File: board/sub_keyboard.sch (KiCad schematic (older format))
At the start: 30 parts, among them SW901 SW_SPST, SW902 SW_SPST, SW903 SW_SPST, SW904 SW_SPST, SW905 SW_SPST, SW906 SW_SPST, SW907 SW_SPST, SW908 SW_SPST, SW909 SW_SPST, SW910 SW_SPST, SW911 SW_SPST, SW912 SW_SPST, SW913 SW_SPST, SW914 SW_SPST, SW915 SW_SPST, SW916 SW_SPST, SW917 SW_SPST, SW918 SW_SPST, SW919 SW_SPST, SW920 SW_SPST, SW921 SW_SPST, SW922 SW_SPST, SW923 SW_SPST, SW924 SW_SPST, SW925 SW_SPST, SW926 SW_SPST, SW927 SW_SPST, SW928 SW_SPST, SW929 SW_SPST, SW930 SW_SPST

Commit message: Started picking footprints. Merged many components.
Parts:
- SW901, SW902, SW903, SW904, SW905, SW906, SW907, SW908, SW909, SW910, SW911, SW912, SW913, SW914, SW915, SW916, SW917, SW918, SW919, SW920, SW921, SW922, SW923, SW924, SW925, SW926, SW927, SW928, SW929, SW930: footprint (none) -> Button_Switch_Keyboard:SW_Cherry_MX1A_1.00u_PCB
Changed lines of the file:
@@
 $Descr A4 11693 8268
 encoding utf-8
-Sheet 9 14
+Sheet 9 15
 Title ""
 Date ""
@@
 F 0 "SW901" H 4500 2450 50  0000 L CNN
 F 1 "SW_SPST" H 4450 2350 50  0001 L CNN
-F 2 "" H 4600 2500 50  0001 C CNN
+F 2 "Button_Switch_Keyboard:SW_Cherry_MX1A_1.00u_PCB" H 4600 2500 50  0001 C CNN
 F 3 "" H 4600 2500 50  0001 C CNN
 	1    4600 2500
@@
 F 0 "SW902" H 5150 2450 50  0000 L CNN
 F 1 "SW_SPST" H 5100 2350 50  0001 L CNN
-F 2 "" H 5250 2500 50  0001 C CNN
+F 2 "Button_Switch_Keyboard:SW_Cherry_MX1A_1.00u_PCB" H 5250 2500 50  0001 C CNN
 F 3 "" H 5250 2500 50  0001 C CNN
 	1    5250 2500
@@
 F 0 "SW903" H 5800 2450 50  0000 L CNN
 F 1 "SW_SPST" H 5750 2350 50  0001 L CNN
-F 2 "" H 5900 2500 50  0001 C CNN
+F 2 "Button_Switch_Keyboard:SW_Cherry_MX1A_1.00u_PCB" H 5900 2500 50  0001 C CNN
 F 3 "" H 5900 2500 50  0001 C CNN
 	1    5900 2500
@@
 F 0 "SW904" H 6450 2450 50  0000 L CNN
 F 1 "SW_SPST" H 6400 2350 50  0001 L CNN
-F 2 "" H 6550 2500 50  0001 C CNN
+F 2 "Button_Switch_Keyboard:SW_Cherry_MX1A_1.00u_PCB" H 6550 2500 50  0001 C CNN
 F 3 "" H 6550 2500 50  0001 C CNN
 	1    6550 2500
@@
 F 0 "SW905" H 7100 2450 50  0000 L CNN
 F 1 "SW_SPST" H 7050 2350 50  0001 L CNN
-F 2 "" H 7200 2500 50  0001 C CNN
+F 2 "Button_Switch_Keyboard:SW_Cherry_MX1A_1.00u_PCB" H 7200 2500 50  0001 C CNN
 F 3 "" H 7200 2500 50  0001 C CNN
 	1    7200 2500
@@
 F 0 "SW906" H 7750 2450 50  0000 L CNN
 F 1 "SW_SPST" H 7700 2350 50  0001 L CNN
-F 2 "" H 7850 2500 50  0001 C CNN
+F 2 "Button_Switch_Keyboard:SW_Cherry_MX1A_1.00u_PCB" H 7850 2500 50  0001 C CNN
 F 3 "" H 7850 2500 50  0001 C CNN
 	1    7850 2500
@@
 F 0 "SW907" H 4500 3000 50  0000 L CNN
 F 1 "SW_SPST" H 4450 2900 50  0001 L CNN
-F 2 "" H 4600 3050 50  0001 C CNN
+F 2 "Button_Switch_Keyboard:SW_Cherry_MX1A_1.00u_PCB" H 4600 3050 50  0001 C CNN
 F 3 "" H 4600 3050 50  0001 C CNN
 	1    4600 3050
@@
 F 0 "SW908" H 5150 3000 50  0000 L CNN
 F 1 "SW_SPST" H 5100 2900 50  0001 L CNN
-F 2 "" H 5250 3050 50  0001 C CNN
+F 2 "Button_Switch_Keyboard:SW_Cherry_MX1A_1.00u_PCB" H 5250 3050 50  0001 C CNN
 F 3 "" H 5250 3050 50  0001 C CNN
 	1    5250 3050
@@
 F 0 "SW909" H 5800 3000 50  0000 L CNN
 F 1 "SW_SPST" H 5750 2900 50  0001 L CNN
-F 2 "" H 5900 3050 50  0001 C CNN
+F 2 "Button_Switch_Keyboard:SW_Cherry_MX1A_1.00u_PCB" H 5900 3050 50  0001 C CNN
 F 3 "" H 5900 3050 50  0001 C CNN
 	1    5900 3050
@@
 F 0 "SW910" H 6450 3000 50  0000 L CNN
 F 1 "SW_SPST" H 6400 2900 50  0001 L CNN
-F 2 "" H 6550 3050 50  0001 C CNN
+F 2 "Button_Switch_Keyboard:SW_Cherry_MX1A_1.00u_PCB" H 6550 3050 50  0001 C CNN
 F 3 "" H 6550 3050 50  0001 C CNN
 	1    6550 3050
@@
 F 0 "SW911" H 7100 3000 50  0000 L CNN
 F 1 "SW_SPST" H 7050 2900 50  0001 L CNN
-F 2 "" H 7200 3050 50  0001 C CNN
+F 2 "Button_Switch_Keyboard:SW_Cherry_MX1A_1.00u_PCB" H 7200 3050 50  0001 C CNN
 F 3 "" H 7200 3050 50  0001 C CNN
 	1    7200 3050
@@
 F 0 "SW912" H 7750 3000 50  0000 L CNN
 F 1 "SW_SPST" H 7700 2900 50  0001 L CNN
-F 2 "" H 7850 3050 50  0001 C CNN
+F 2 "Button_Switch_Keyboard:SW_Cherry_MX1A_1.00u_PCB" H 7850 3050 50  0001 C CNN
 F 3 "" H 7850 3050 50  0001 C CNN
 	1    7850 3050
@@
 F 0 "SW913" H 4500 3550 50  0000 L CNN
 F 1 "SW_SPST" H 4450 3450 50  0001 L CNN
-F 2 "" H 4600 3600 50  0001 C CNN
+F 2 "Button_Switch_Keyboard:SW_Cherry_MX1A_1.00u_PCB" H 4600 3600 50  0001 C CNN
 F 3 "" H 4600 3600 50  0001 C CNN
 	1    4600 3600
@@
 F 0 "SW914" H 5150 3550 50  0000 L CNN
 F 1 "SW_SPST" H 5100 3450 50  0001 L CNN
-F 2 "" H 5250 3600 50  0001 C CNN
+F 2 "Button_Switch_Keyboard:SW_Cherry_MX1A_1.00u_PCB" H 5250 3600 50  0001 C CNN
 F 3 "" H 5250 3600 50  0001 C CNN
 	1    5250 3600
@@
 F 0 "SW915" H 5800 3550 50  0000 L CNN
 F 1 "SW_SPST" H 5750 3450 50  0001 L CNN
-F 2 "" H 5900 3600 50  0001 C CNN
+F 2 "Button_Switch_Keyboard:SW_Cherry_MX1A_1.00u_PCB" H 5900 3600 50  0001 C CNN
 F 3 "" H 5900 3600 50  0001 C CNN
 	1    5900 3600
@@
 F 0 "SW916" H 6450 3550 50  0000 L CNN
 F 1 "SW_SPST" H 6400 3450 50  0001 L CNN
-F 2 "" H 6550 3600 50  0001 C CNN
+F 2 "Button_Switch_Keyboard:SW_Cherry_MX1A_1.00u_PCB" H 6550 3600 50  0001 C CNN
 F 3 "" H 6550 3600 50  0001 C CNN
 	1    6550 3600
@@
 F 0 "SW917" H 7100 3550 50  0000 L CNN
 F 1 "SW_SPST" H 7050 3450 50  0001 L CNN
-F 2 "" H 7200 3600 50  0001 C CNN
+F 2 "Button_Switch_Keyboard:SW_Cherry_MX1A_1.00u_PCB" H 7200 3600 50  0001 C CNN
 F 3 "" H 7200 3600 50  0001 C CNN
 	1    7200 3600
@@
 F 0 "SW918" H 7750 3550 50  0000 L CNN
 F 1 "SW_SPST" H 7700 3450 50  0001 L CNN
-F 2 "" H 7850 3600 50  0001 C CNN
+F 2 "Button_Switch_Keyboard:SW_Cherry_MX1A_1.00u_PCB" H 7850 3600 50  0001 C CNN
 F 3 "" H 7850 3600 50  0001 C CNN
 	1    7850 3600
@@
 F 0 "SW919" H 4500 4100 50  0000 L CNN
 F 1 "SW_SPST" H 4450 4000 50  0001 L CNN
-F 2 "" H 4600 4150 50  0001 C CNN
+F 2 "Button_Switch_Keyboard:SW_Cherry_MX1A_1.00u_PCB" H 4600 4150 50  0001 C CNN
 F 3 "" H 4600 4150 50  0001 C CNN
 	1    4600 4150
@@
 F 0 "SW920" H 5150 4100 50  0000 L CNN
 F 1 "SW_SPST" H 5100 4000 50  0001 L CNN
-F 2 "" H 5250 4150 50  0001 C CNN
+F 2 "Button_Switch_Keyboard:SW_Cherry_MX1A_1.00u_PCB" H 5250 4150 50  0001 C CNN
 F 3 "" H 5250 4150 50  0001 C CNN
 	1    5250 4150
@@
 F 0 "SW921" H 5800 4100 50  0000 L CNN
 F 1 "SW_SPST" H 5750 4000 50  0001 L CNN
-F 2 "" H 5900 4150 50  0001 C CNN
+F 2 "Button_Switch_Keyboard:SW_Cherry_MX1A_1.00u_PCB" H 5900 4150 50  0001 C CNN
 F 3 "" H 5900 4150 50  0001 C CNN
 	1    5900 4150
@@
 F 0 "SW922" H 6450 4100 50  0000 L CNN
 F 1 "SW_SPST" H 6400 4000 50  0001 L CNN
-F 2 "" H 6550 4150 50  0001 C CNN
+F 2 "Button_Switch_Keyboard:SW_Cherry_MX1A_1.00u_PCB" H 6550 4150 50  0001 C CNN
 F 3 "" H 6550 4150 50  0001 C CNN
 	1    6550 4150
@@
 F 0 "SW923" H 7100 4100 50  0000 L CNN
 F 1 "SW_SPST" H 7050 4000 50  0001 L CNN
-F 2 "" H 7200 4150 50  0001 C CNN
+F 2 "Button_Switch_Keyboard:SW_Cherry_MX1A_1.00u_PCB" H 7200 4150 50  0001 C CNN
 F 3 "" H 7200 4150 50  0001 C CNN
 	1    7200 4150
@@
 F 0 "SW924" H 7750 4100 50  0000 L CNN
 F 1 "SW_SPST" H 7700 4000 50  0001 L CNN
-F 2 "" H 7850 4150 50  0001 C CNN
+F 2 "Button_Switch_Keyboard:SW_Cherry_MX1A_1.00u_PCB" H 7850 4150 50  0001 C CNN
 F 3 "" H 7850 4150 50  0001 C CNN
 	1    7850 4150
@@
 F 0 "SW925" H 4500 4650 50  0000 L CNN
 F 1 "SW_SPST" H 4450 4550 50  0001 L CNN
-F 2 "" H 4600 4700 50  0001 C CNN
+F 2 "Button_Switch_Keyboard:SW_Cherry_MX1A_1.00u_PCB" H 4600 4700 50  0001 C CNN
 F 3 "" H 4600 4700 50  0001 C CNN
 	1    4600 4700
@@
 F 0 "SW926" H 5150 4650 50  0000 L CNN
 F 1 "SW_SPST" H 5100 4550 50  0001 L CNN
-F 2 "" H 5250 4700 50  0001 C CNN
+F 2 "Button_Switch_Keyboard:SW_Cherry_MX1A_1.00u_PCB" H 5250 4700 50  0001 C CNN
 F 3 "" H 5250 4700 50  0001 C CNN
 	1    5250 4700
@@
 F 0 "SW927" H 5800 4650 50  0000 L CNN
 F 1 "SW_SPST" H 5750 4550 50  0001 L CNN
-F 2 "" H 5900 4700 50  0001 C CNN
+F 2 "Button_Switch_Keyboard:SW_Cherry_MX1A_1.00u_PCB" H 5900 4700 50  0001 C CNN
 F 3 "" H 5900 4700 50  0001 C CNN
 	1    5900 4700
@@
 F 0 "SW928" H 6450 4650 50  0000 L CNN
 F 1 "SW_SPST" H 6400 4550 50  0001 L CNN
-F 2 "" H 6550 4700 50  0001 C CNN
+F 2 "Button_Switch_Keyboard:SW_Cherry_MX1A_1.00u_PCB" H 6550 4700 50  0001 C CNN
 F 3 "" H 6550 4700 50  0001 C CNN
 	1    6550 4700
@@
 F 0 "SW929" H 7100 4650 50  0000 L CNN
 F 1 "SW_SPST" H 7050 4550 50  0001 L CNN
-F 2 "" H 7200 4700 50  0001 C CNN
+F 2 "Button_Switch_Keyboard:SW_Cherry_MX1A_1.00u_PCB" H 7200 4700 50  0001 C CNN
 F 3 "" H 7200 4700 50  0001 C CNN
 	1    7200 4700
@@
 F 0 "SW930" H 7750 4650 50  0000 L CNN
 F 1 "SW_SPST" H 7700 4550 50  0001 L CNN
-F 2 "" H 7850 4700 50  0001 C CNN
+F 2 "Button_Switch_Keyboard:SW_Cherry_MX1A_1.00u_PCB" H 7850 4700 50  0001 C CNN
 F 3 "" H 7850 4700 50  0001 C CNN
 	1    7850 4700

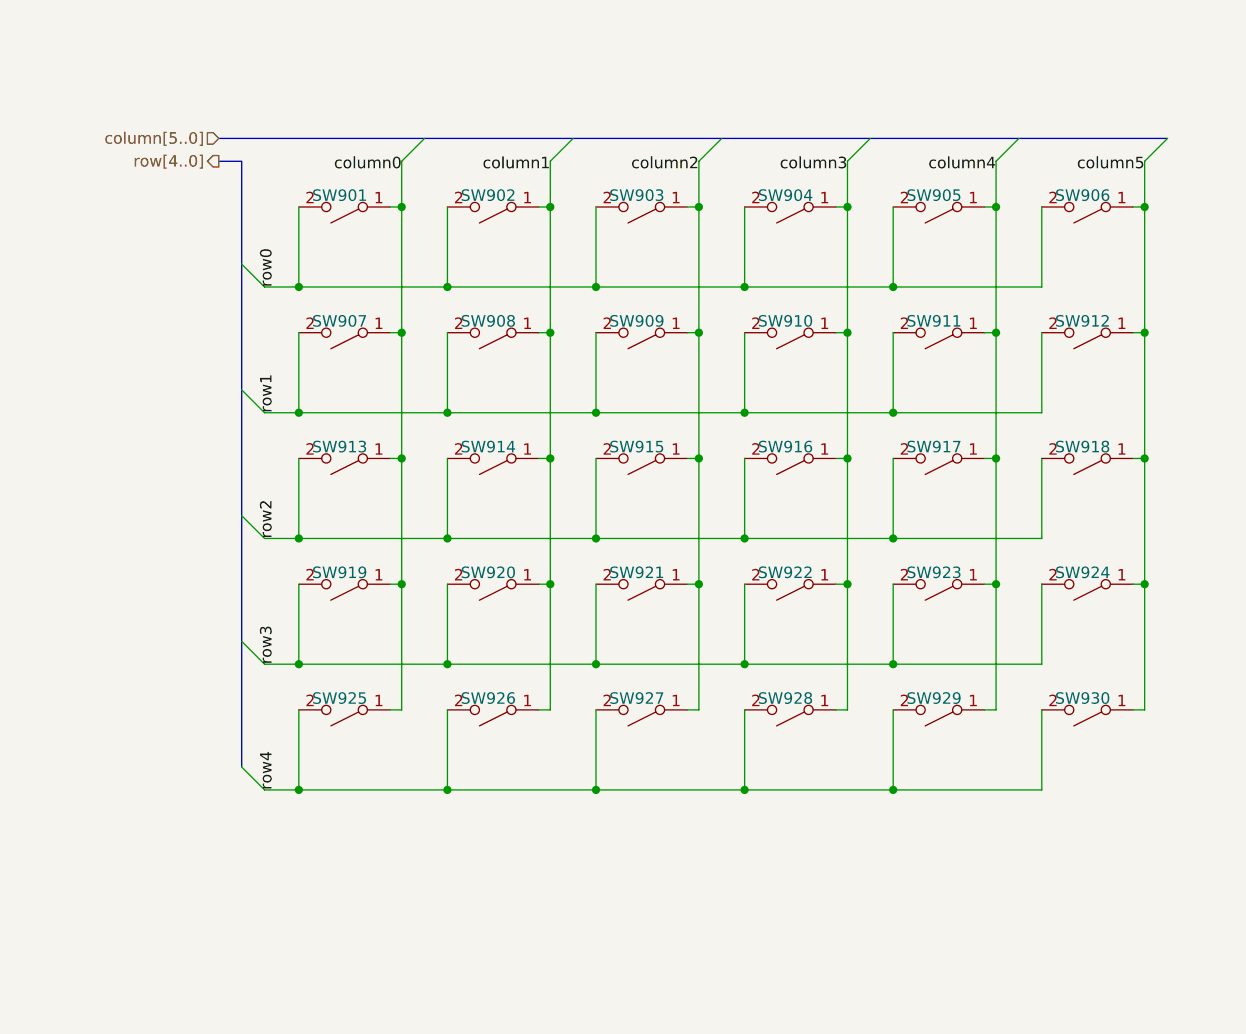
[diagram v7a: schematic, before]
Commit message: Power supply routed
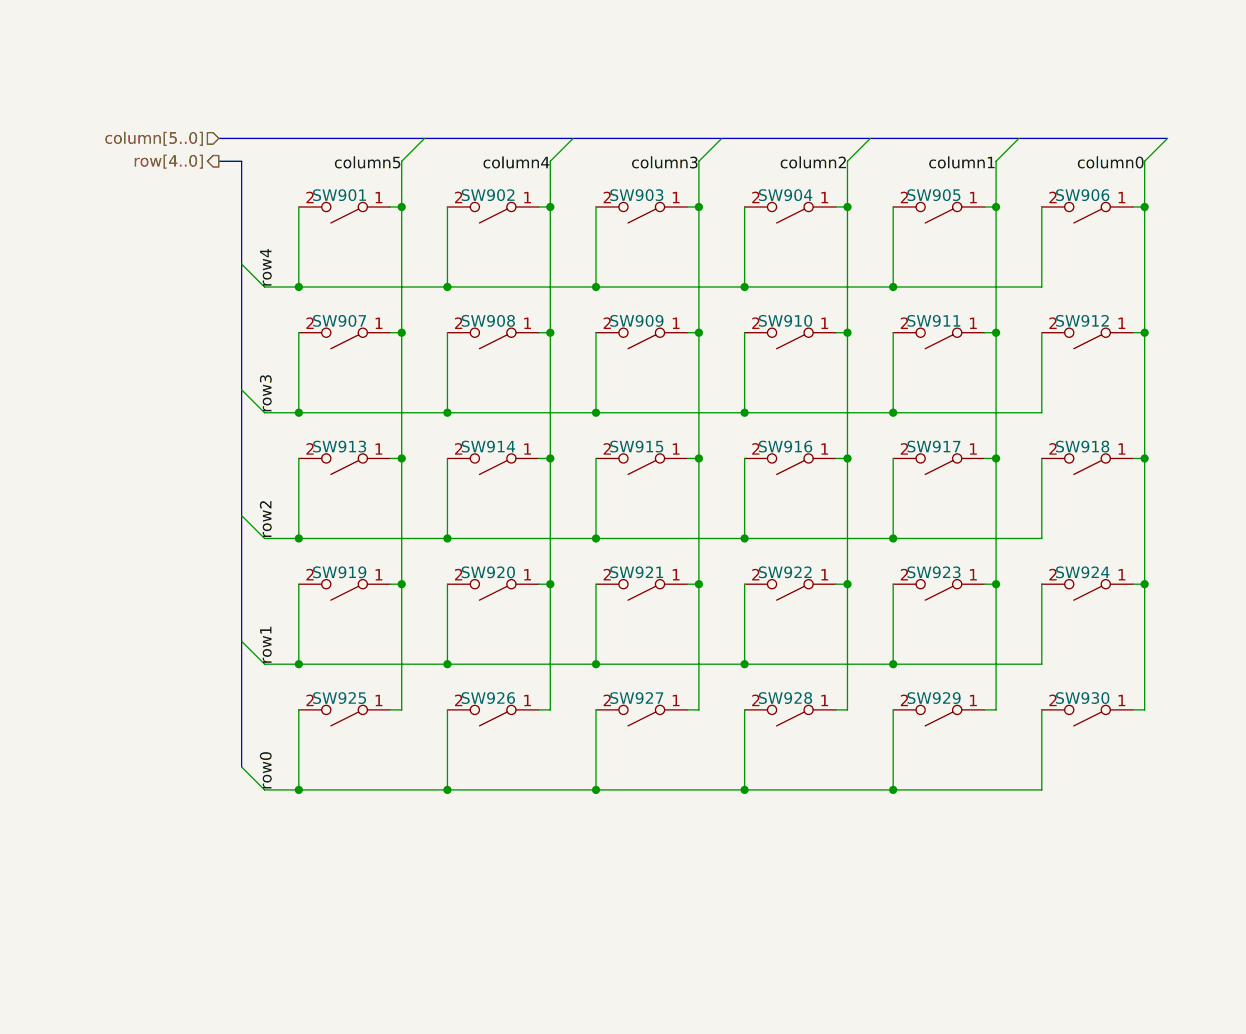
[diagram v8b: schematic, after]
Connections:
- net column0: now also SW906.1 (A), SW912.1 (A), SW918.1 (A), SW924.1 (A), SW930.1 (A); no longer SW901.1 (A), SW907.1 (A), SW913.1 (A), SW919.1 (A), SW925.1 (A)
- net column1: now also SW905.1 (A), SW911.1 (A), SW917.1 (A), SW923.1 (A), SW929.1 (A); no longer SW902.1 (A), SW908.1 (A), SW914.1 (A), SW920.1 (A), SW926.1 (A)
- net column2: now also SW904.1 (A), SW910.1 (A), SW916.1 (A), SW922.1 (A), SW928.1 (A); no longer SW903.1 (A), SW909.1 (A), SW915.1 (A), SW921.1 (A), SW927.1 (A)
- net column3: now also SW903.1 (A), SW909.1 (A), SW915.1 (A), SW921.1 (A), SW927.1 (A); no longer SW904.1 (A), SW910.1 (A), SW916.1 (A), SW922.1 (A), SW928.1 (A)
- net column4: now also SW902.1 (A), SW908.1 (A), SW914.1 (A), SW920.1 (A), SW926.1 (A); no longer SW905.1 (A), SW911.1 (A), SW917.1 (A), SW923.1 (A), SW929.1 (A)
- net column5: now also SW901.1 (A), SW907.1 (A), SW913.1 (A), SW919.1 (A), SW925.1 (A); no longer SW906.1 (A), SW912.1 (A), SW918.1 (A), SW924.1 (A), SW930.1 (A)
- net row0: now also SW925.2 (B), SW926.2 (B), SW927.2 (B), SW928.2 (B), SW929.2 (B), SW930.2 (B); no longer SW901.2 (B), SW902.2 (B), SW903.2 (B), SW904.2 (B), SW905.2 (B), SW906.2 (B)
- net row1: now also SW919.2 (B), SW920.2 (B), SW921.2 (B), SW922.2 (B), SW923.2 (B), SW924.2 (B); no longer SW907.2 (B), SW908.2 (B), SW909.2 (B), SW910.2 (B), SW911.2 (B), SW912.2 (B)
- net row3: now also SW907.2 (B), SW908.2 (B), SW909.2 (B), SW910.2 (B), SW911.2 (B), SW912.2 (B); no longer SW919.2 (B), SW920.2 (B), SW921.2 (B), SW922.2 (B), SW923.2 (B), SW924.2 (B)
- net row4: now also SW901.2 (B), SW902.2 (B), SW903.2 (B), SW904.2 (B), SW905.2 (B), SW906.2 (B); no longer SW925.2 (B), SW926.2 (B), SW927.2 (B), SW928.2 (B), SW929.2 (B), SW930.2 (B)
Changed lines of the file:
@@
 Entry Wire Line
 	8100 2300 8200 2200
+Text Label 8100 2350 2    50   ~ 0
+column0
+Text Label 7450 2350 2    50   ~ 0
+column1
+Text Label 6800 2350 2    50   ~ 0
+column2
+Text Label 6150 2350 2    50   ~ 0
+column3
+Text Label 5500 2350 2    50   ~ 0
+column4
 Text Label 4850 2350 2    50   ~ 0
-column0
-Text Label 5500 2350 2    50   ~ 0
-column1
-Text Label 6150 2350 2    50   ~ 0
-column2
-Text Label 6800 2350 2    50   ~ 0
-column3
-Text Label 7450 2350 2    50   ~ 0
-column4
-Text Label 8100 2350 2    50   ~ 0
 column5
 Entry Wire Line
@@
 Wire Bus Line
 	4150 2300 4050 2300
-Text Label 4300 2850 1    50   ~ 0
+Text Label 4300 5050 1    50   ~ 0
 row0
-Text Label 4300 3400 1    50   ~ 0
+Text Label 4300 4500 1    50   ~ 0
 row1
 Text Label 4300 3950 1    50   ~ 0
 row2
-Text Label 4300 4500 1    50   ~ 0
+Text Label 4300 3400 1    50   ~ 0
 row3
-Text Label 4300 5050 1    50   ~ 0
+Text Label 4300 2850 1    50   ~ 0
 row4
 Wire Wire Line
